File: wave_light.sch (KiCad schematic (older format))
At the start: 18 parts, among them J1 Conn_01x02_Male, J2 Conn_01x02_Female, J3 Conn_01x02_Female, J4 Conn_01x02_Female, J5 Conn_01x02_Female, J6 Conn_01x02_Female, J7 Conn_01x02_Female, J8 Conn_01x02_Female, J9 Conn_01x02_Female

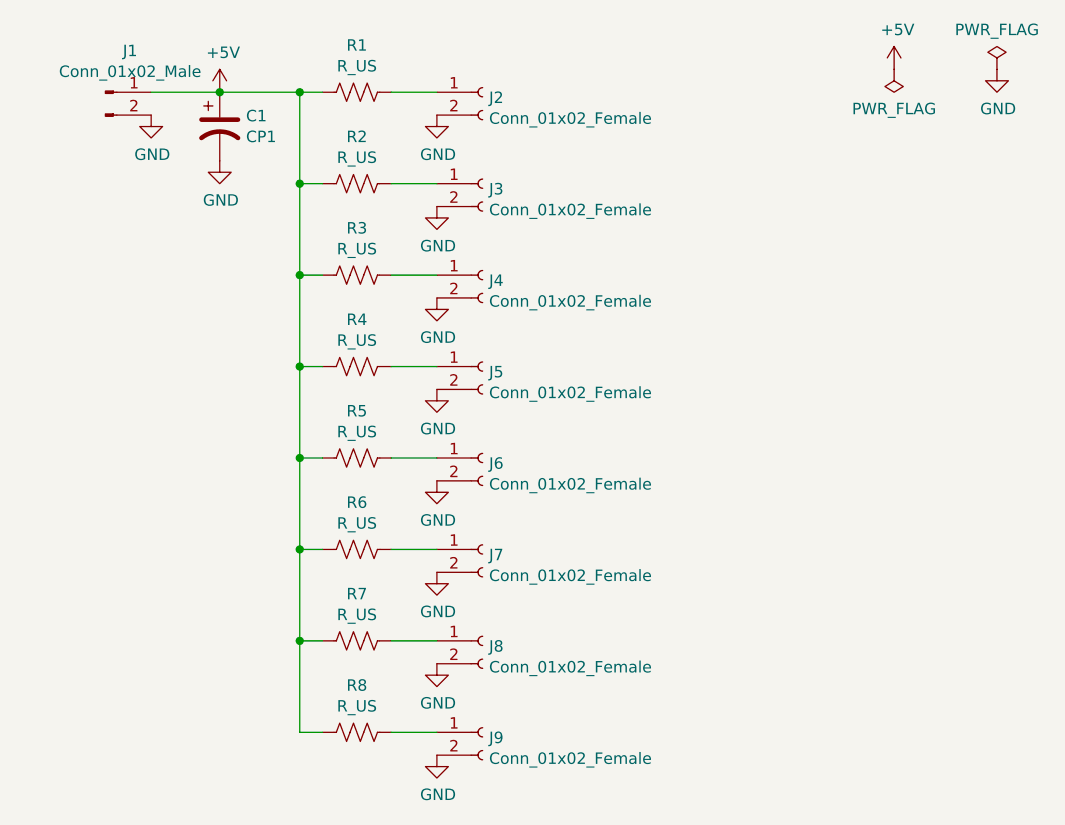
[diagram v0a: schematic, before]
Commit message: Redesign with rectangular layout
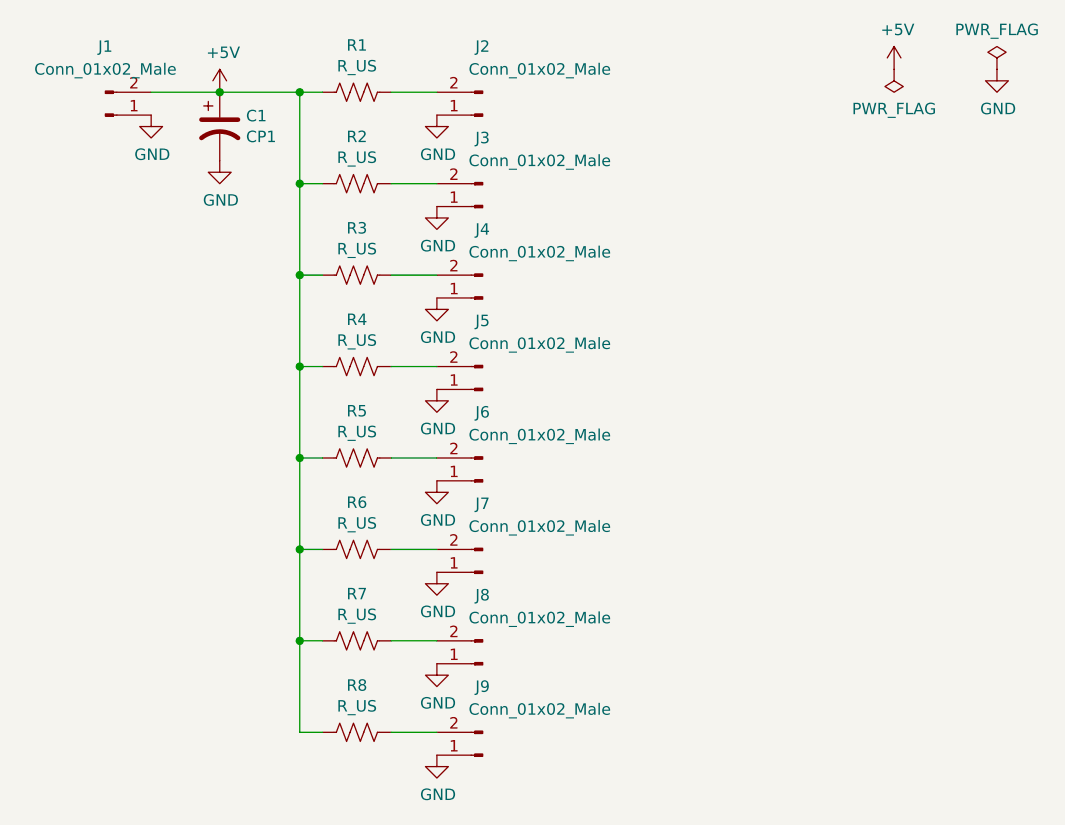
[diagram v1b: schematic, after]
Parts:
- removed J2, J3, J4, J5, J6, J7, J8, J9: Conn_01x02_Female, Connector_PinSocket_2.54mm:PinSocket_1x02_P2.54mm_Vertical, symbol Connector:Conn_01x02_Female
- added J2, J3, J4, J5, J6, J7, J8, J9: Conn_01x02_Male, Connector_JST:JST_XH_B2B-XH-A_1x02_P2.50mm_Vertical, symbol Connector:Conn_01x02_Male
- J1: footprint Connector_PinHeader_2.54mm:PinHeader_1x02_P2.54mm_Vertical -> Connector_JST:JST_XH_B2B-XH-A_1x02_P2.50mm_Vertical
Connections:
- net +5V: now also J1.2 (Pin_2); no longer J1.1 (Pin_1)
- net GND: now also J1.1 (Pin_1), J2.1 (Pin_1), J3.1 (Pin_1), J4.1 (Pin_1), J5.1 (Pin_1), J6.1 (Pin_1), J7.1 (Pin_1), J8.1 (Pin_1), J9.1 (Pin_1); no longer J1.2 (Pin_2)
- net at R1.1: now also J2.2 (Pin_2)
- net at R2.1: now also J3.2 (Pin_2)
- net at R3.1: now also J4.2 (Pin_2)
- net at R4.1: now also J5.2 (Pin_2)
- net at R5.1: now also J6.2 (Pin_2)
- net at R6.1: now also J7.2 (Pin_2)
- net at R7.1: now also J8.2 (Pin_2)
- net at R8.1: now also J9.2 (Pin_2)
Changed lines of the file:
@@
 L Connector:Conn_01x02_Male J1
 U 1 1 5ED5295D
-P 3200 1300
-F 0 "J1" H 3308 1481 50  0000 C CNN
-F 1 "Conn_01x02_Male" H 3308 1390 50  0000 C CNN
-F 2 "Connector_PinHeader_2.54mm:PinHeader_1x02_P2.54mm_Vertical" H 3200 1300 50  0001 C CNN
-F 3 "~" H 3200 1300 50  0001 C CNN
-	1    3200 1300
-	1    0    0    -1
+P 3200 1400
+F 0 "J1" H 3200 1100 50  0000 C CNN
+F 1 "Conn_01x02_Male" H 3200 1200 50  0000 C CNN
+F 2 "Connector_JST:JST_XH_B2B-XH-A_1x02_P2.50mm_Vertical" H 3200 1400 50  0001 C CNN
+F 3 "~" H 3200 1400 50  0001 C CNN
+	1    3200 1400
+	1    0    0    1
 $EndComp
 $Comp
@@
 $EndComp
 $Comp
-L Connector:Conn_01x02_Female J2
-U 1 1 5ED5C3A8
-P 4850 1300
-F 0 "J2" H 4878 1276 50  0000 L CNN
-F 1 "Conn_01x02_Female" H 4878 1185 50  0000 L CNN
-F 2 "Connector_PinSocket_2.54mm:PinSocket_1x02_P2.54mm_Vertical" H 4850 1300 50  0001 C CNN
-F 3 "~" H 4850 1300 50  0001 C CNN
-	1    4850 1300
-	1    0    0    -1
-$EndComp
-$Comp
-L Connector:Conn_01x02_Female J3
-U 1 1 5ED5D0A8
-P 4850 1700
-F 0 "J3" H 4878 1676 50  0000 L CNN
-F 1 "Conn_01x02_Female" H 4878 1585 50  0000 L CNN
-F 2 "Connector_PinSocket_2.54mm:PinSocket_1x02_P2.54mm_Vertical" H 4850 1700 50  0001 C CNN
-F 3 "~" H 4850 1700 50  0001 C CNN
-	1    4850 1700
-	1    0    0    -1
-$EndComp
-$Comp
-L Connector:Conn_01x02_Female J4
-U 1 1 5ED5D708
-P 4850 2100
-F 0 "J4" H 4878 2076 50  0000 L CNN
-F 1 "Conn_01x02_Female" H 4878 1985 50  0000 L CNN
-F 2 "Connector_PinSocket_2.54mm:PinSocket_1x02_P2.54mm_Vertical" H 4850 2100 50  0001 C CNN
-F 3 "~" H 4850 2100 50  0001 C CNN
-	1    4850 2100
-	1    0    0    -1
-$EndComp
-$Comp
-L Connector:Conn_01x02_Female J5
-U 1 1 5ED5DCEC
-P 4850 2500
-F 0 "J5" H 4878 2476 50  0000 L CNN
-F 1 "Conn_01x02_Female" H 4878 2385 50  0000 L CNN
-F 2 "Connector_PinSocket_2.54mm:PinSocket_1x02_P2.54mm_Vertical" H 4850 2500 50  0001 C CNN
-F 3 "~" H 4850 2500 50  0001 C CNN
-	1    4850 2500
-	1    0    0    -1
-$EndComp
-$Comp
-L Connector:Conn_01x02_Female J6
-U 1 1 5ED5E5A3
-P 4850 2900
-F 0 "J6" H 4878 2876 50  0000 L CNN
-F 1 "Conn_01x02_Female" H 4878 2785 50  0000 L CNN
-F 2 "Connector_PinSocket_2.54mm:PinSocket_1x02_P2.54mm_Vertical" H 4850 2900 50  0001 C CNN
-F 3 "~" H 4850 2900 50  0001 C CNN
-	1    4850 2900
-	1    0    0    -1
-$EndComp
-$Comp
-L Connector:Conn_01x02_Female J7
-U 1 1 5ED5EEEE
-P 4850 3300
-F 0 "J7" H 4878 3276 50  0000 L CNN
-F 1 "Conn_01x02_Female" H 4878 3185 50  0000 L CNN
-F 2 "Connector_PinSocket_2.54mm:PinSocket_1x02_P2.54mm_Vertical" H 4850 3300 50  0001 C CNN
-F 3 "~" H 4850 3300 50  0001 C CNN
-	1    4850 3300
-	1    0    0    -1
-$EndComp
-$Comp
-L Connector:Conn_01x02_Female J8
-U 1 1 5ED5FDA6
-P 4850 3700
-F 0 "J8" H 4878 3676 50  0000 L CNN
-F 1 "Conn_01x02_Female" H 4878 3585 50  0000 L CNN
-F 2 "Connector_PinSocket_2.54mm:PinSocket_1x02_P2.54mm_Vertical" H 4850 3700 50  0001 C CNN
-F 3 "~" H 4850 3700 50  0001 C CNN
-	1    4850 3700
-	1    0    0    -1
-$EndComp
-$Comp
-L Connector:Conn_01x02_Female J9
-U 1 1 5ED60228
-P 4850 4100
-F 0 "J9" H 4878 4076 50  0000 L CNN
-F 1 "Conn_01x02_Female" H 4878 3985 50  0000 L CNN
-F 2 "Connector_PinSocket_2.54mm:PinSocket_1x02_P2.54mm_Vertical" H 4850 4100 50  0001 C CNN
-F 3 "~" H 4850 4100 50  0001 C CNN
-	1    4850 4100
-	1    0    0    -1
-$EndComp
-$Comp
 L power:GND #PWR0101
 U 1 1 5ED60E5E
@@
 	1    0    0    -1
 $EndComp
+$Comp
+L Connector:Conn_01x02_Male J2
+U 1 1 5EE00D95
+P 4850 1400
+F 0 "J2" H 4850 1100 50  0000 C CNN
+F 1 "Conn_01x02_Male" H 4600 1200 50  0000 C CNN
+F 2 "Connector_JST:JST_XH_B2B-XH-A_1x02_P2.50mm_Vertical" H 4850 1400 50  0001 C CNN
+F 3 "~" H 4850 1400 50  0001 C CNN
+	1    4850 1400
+	-1   0    0    1
+$EndComp
+$Comp
+L Connector:Conn_01x02_Male J3
+U 1 1 5EE2D0D4
+P 4850 1800
+F 0 "J3" H 4850 1500 50  0000 C CNN
+F 1 "Conn_01x02_Male" H 4600 1600 50  0000 C CNN
+F 2 "Connector_JST:JST_XH_B2B-XH-A_1x02_P2.50mm_Vertical" H 4850 1800 50  0001 C CNN
+F 3 "~" H 4850 1800 50  0001 C CNN
+	1    4850 1800
+	-1   0    0    1
+$EndComp
+$Comp
+L Connector:Conn_01x02_Male J4
+U 1 1 5EE2E5CE
+P 4850 2200
+F 0 "J4" H 4850 1900 50  0000 C CNN
+F 1 "Conn_01x02_Male" H 4600 2000 50  0000 C CNN
+F 2 "Connector_JST:JST_XH_B2B-XH-A_1x02_P2.50mm_Vertical" H 4850 2200 50  0001 C CNN
+F 3 "~" H 4850 2200 50  0001 C CNN
+	1    4850 2200
+	-1   0    0    1
+$EndComp
+$Comp
+L Connector:Conn_01x02_Male J5
+U 1 1 5EE2E5D8
+P 4850 2600
+F 0 "J5" H 4850 2300 50  0000 C CNN
+F 1 "Conn_01x02_Male" H 4600 2400 50  0000 C CNN
+F 2 "Connector_JST:JST_XH_B2B-XH-A_1x02_P2.50mm_Vertical" H 4850 2600 50  0001 C CNN
+F 3 "~" H 4850 2600 50  0001 C CNN
+	1    4850 2600
+	-1   0    0    1
+$EndComp
+$Comp
+L Connector:Conn_01x02_Male J6
+U 1 1 5EE2FC9C
+P 4850 3000
+F 0 "J6" H 4850 2700 50  0000 C CNN
+F 1 "Conn_01x02_Male" H 4600 2800 50  0000 C CNN
+F 2 "Connector_JST:JST_XH_B2B-XH-A_1x02_P2.50mm_Vertical" H 4850 3000 50  0001 C CNN
+F 3 "~" H 4850 3000 50  0001 C CNN
+	1    4850 3000
+	-1   0    0    1
+$EndComp
+$Comp
+L Connector:Conn_01x02_Male J7
+U 1 1 5EE2FCA6
+P 4850 3400
+F 0 "J7" H 4850 3100 50  0000 C CNN
+F 1 "Conn_01x02_Male" H 4600 3200 50  0000 C CNN
+F 2 "Connector_JST:JST_XH_B2B-XH-A_1x02_P2.50mm_Vertical" H 4850 3400 50  0001 C CNN
+F 3 "~" H 4850 3400 50  0001 C CNN
+	1    4850 3400
+	-1   0    0    1
+$EndComp
+$Comp
+L Connector:Conn_01x02_Male J8
+U 1 1 5EE2FCB0
+P 4850 3800
+F 0 "J8" H 4850 3500 50  0000 C CNN
+F 1 "Conn_01x02_Male" H 4600 3600 50  0000 C CNN
+F 2 "Connector_JST:JST_XH_B2B-XH-A_1x02_P2.50mm_Vertical" H 4850 3800 50  0001 C CNN
+F 3 "~" H 4850 3800 50  0001 C CNN
+	1    4850 3800
+	-1   0    0    1
+$EndComp
+$Comp
+L Connector:Conn_01x02_Male J9
+U 1 1 5EE2FCBA
+P 4850 4200
+F 0 "J9" H 4850 3900 50  0000 C CNN
+F 1 "Conn_01x02_Male" H 4600 4000 50  0000 C CNN
+F 2 "Connector_JST:JST_XH_B2B-XH-A_1x02_P2.50mm_Vertical" H 4850 4200 50  0001 C CNN
+F 3 "~" H 4850 4200 50  0001 C CNN
+	1    4850 4200
+	-1   0    0    1
+$EndComp
 $EndSCHEMATC
